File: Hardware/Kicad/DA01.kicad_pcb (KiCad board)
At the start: 2 copper layers, 87.6 x 59.7 mm, 27 parts, among them J1 Conn 1x4 pins, J2 Terminal 1x2, J3 Terminal 1x2, J4 Conn 2x3 pins, J5 Terminal 1x8, J6 Terminal 1x2, J7 Conn 1x8 pins, U1 LM7805, U2 6N137, U3 DFPlayerMini

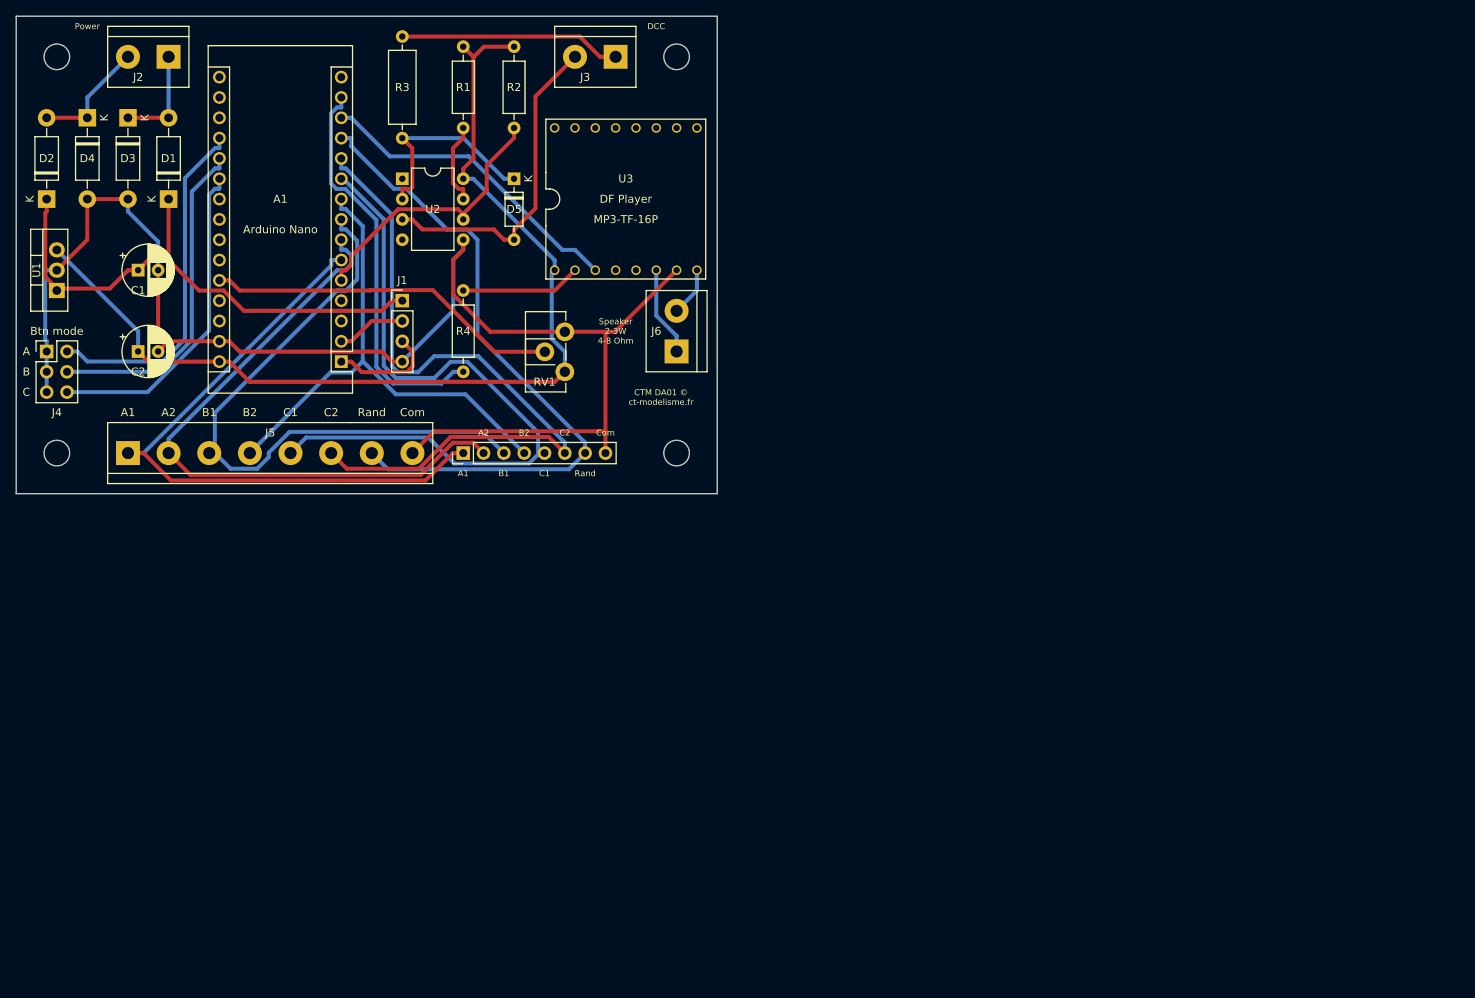
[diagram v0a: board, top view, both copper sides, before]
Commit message: Add CTM in cartridge & PCB
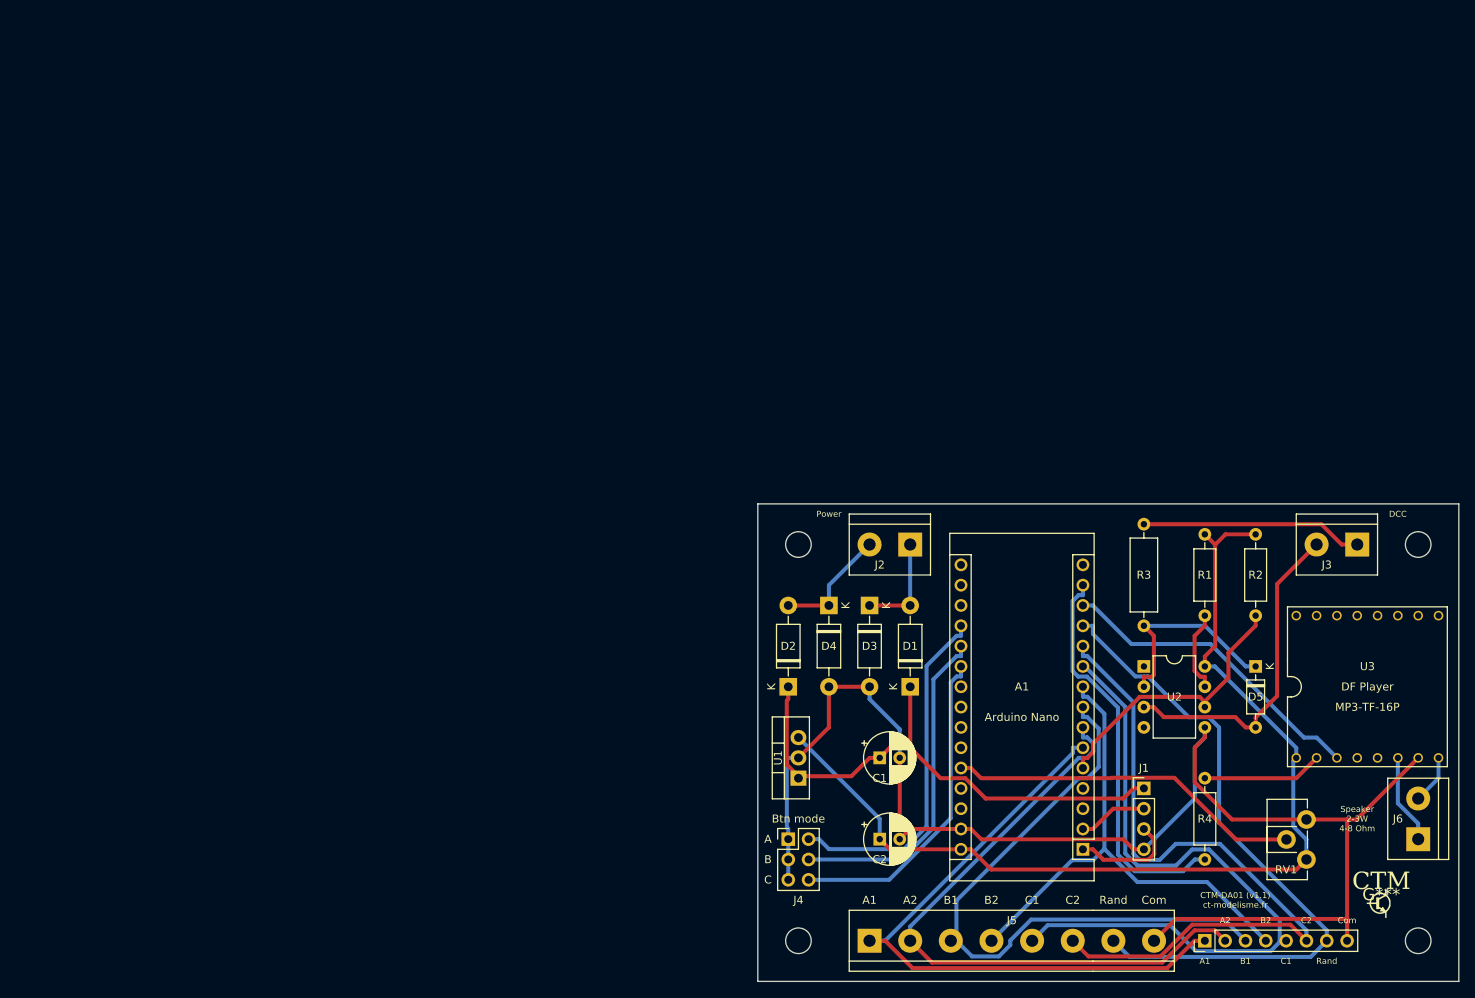
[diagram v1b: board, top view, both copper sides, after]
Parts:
- added G***: LOGO, CTM:Logo_CTM_7mm, F.Cu at (184.6, 123.8)
- moved J1 110.9 mm to (154.9, 110.5)
- moved J7 110.9 mm to (162.6, 129.5)
- moved R1 110.9 mm to (162.6, 78.7)
- moved R3 110.9 mm to (154.9, 90.2)
- moved R4 110.9 mm to (162.6, 109.2)
- moved U2 110.9 mm to (154.9, 95.2)
- moved C1 110.9 mm to (121.9, 106.7)
- moved D1 110.9 mm to (125.7, 97.8)
- moved J2 110.9 mm to (125.7, 80.0)
- moved J3 110.9 mm to (181.6, 80.0)
- moved A1 110.9 mm to (147.3, 118.1)
- moved D2 110.9 mm to (110.5, 97.8)
- moved D3 110.9 mm to (120.6, 87.6)
- moved D4 110.9 mm to (115.6, 87.6)
- moved D5 110.9 mm to (168.9, 95.2)
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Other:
- board text added: "CTM-DA01 (v1.1) ct-modelisme.fr"
- board text removed: "CTM DA01 © ct-modelisme.fr"
